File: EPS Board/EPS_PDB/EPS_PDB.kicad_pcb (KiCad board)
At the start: 4 copper layers, 92 x 92 mm, 126 parts, among them J1 USB_B_Micro, J2 Conn_02x26_Odd_Even, J3 Conn_02x26_Odd_Even, J4 Conn_01x04_Pin, Q1 PMOS, Q2 PMOS, SW1 SW_SPDT, U1 AMS1117-3.3, U10 TPS259621DDAT_5V_PAY, U11 LM5000-3MTCX, U12 TPS259621DDAT_5V_EPS, U13 TPS259621DDAT_5V_OBC, U14 AD7708BRUZ, U15 TPS259621DDAT_5V_ADCS, U16 TPS259621DDAT_5V_COMM, U17 LTC3624EMSE-3.3PBF, U18 TPS259621DDAT_12V_ADCS, U19 LTC3624IDD-25PBF, U2 SN65HVD256D, U3 SN65HVD256D, U4 STM32L476VET6, U5 TPS3824-33QDBVRQ1, U6 TS4061BICT-1.25, U7 TPS259621DDAT 3V3_ADCS, U8 TPS259621DDAT_3V3_ANT, U9 TPS259621DDAT_3V3_EPS, Y1 32MHz, Y2 32.768kHz

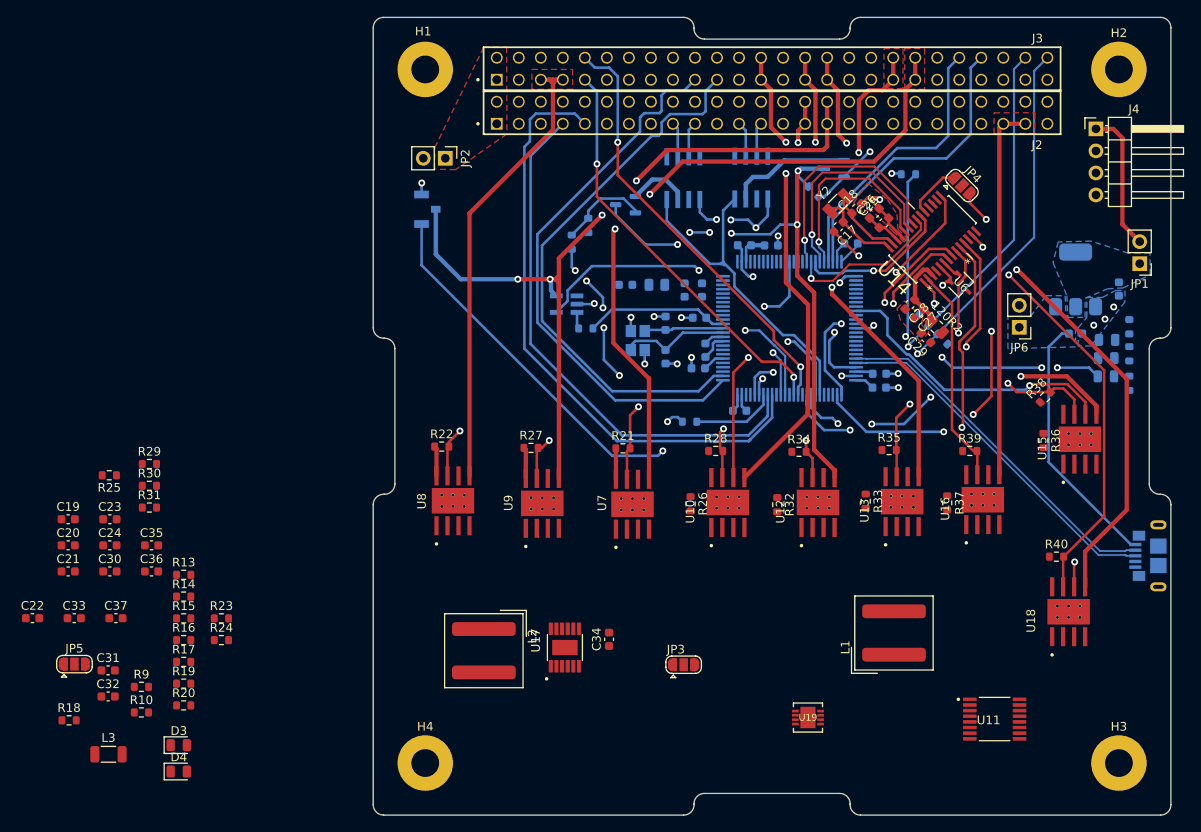
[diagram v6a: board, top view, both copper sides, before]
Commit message: EPS PDB Layout Progress
Voltage Converter layout pending
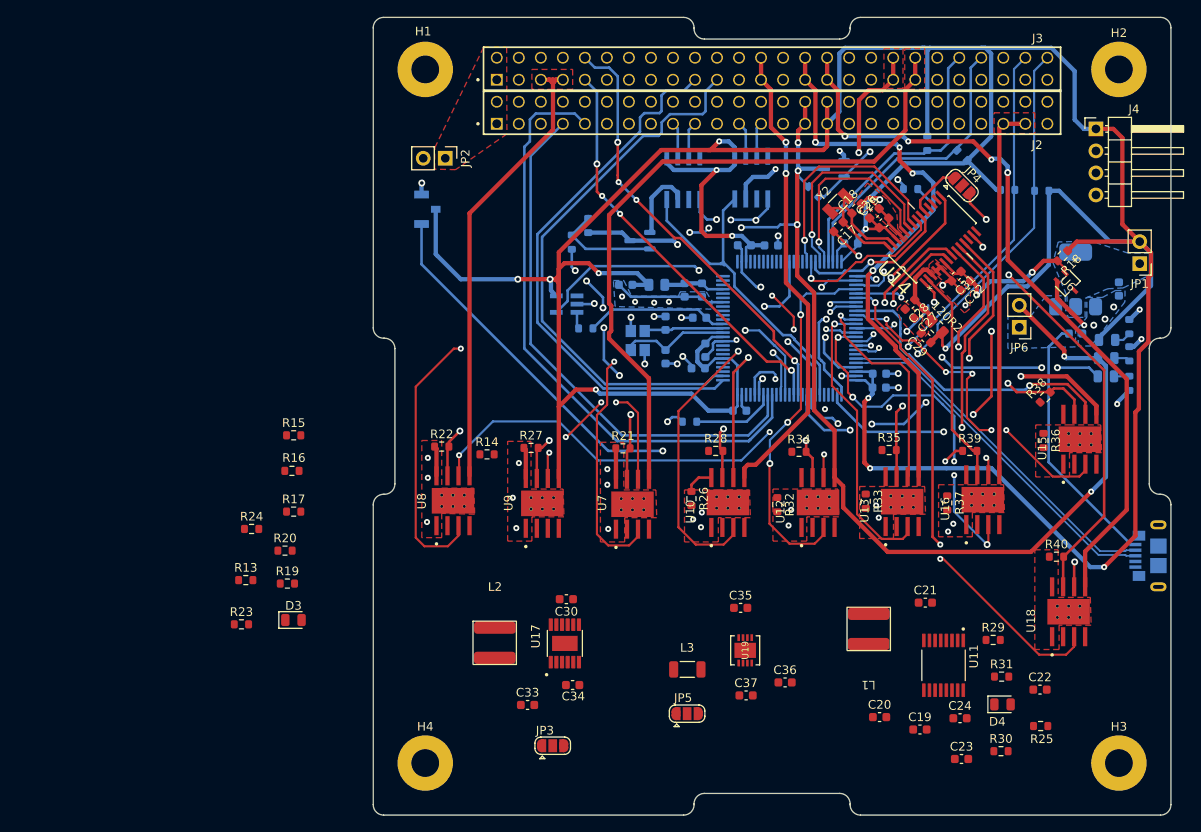
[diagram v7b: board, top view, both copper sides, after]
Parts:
- L1, L2: footprint Inductor_SMD:L_Wuerth_WE-XHMI-8080 -> Inductor-WE-XHMI-5050:WE-XHMI-5050
- R10, R9: moved to B.Cu
- moved R18 126.5 mm to (192.8, 74.2), turned to -135 degrees
- moved C22 116.5 mm to (190.2, 124.2)
- moved R10 114.4 mm to (181.2, 62.6), turned to 135 degrees
- moved R25 111.2 mm to (190.3, 128.4)
- moved R9 110.2 mm to (177.2, 61.2), turned to -90 degrees
- moved C32 109.7 mm to (181.6, 77.6), turned to -135 degrees
- moved C31 107.9 mm to (180.5, 76.5), turned to -135 degrees
- moved R30 102.9 mm to (185.7, 131.3)
- moved C23 102.0 mm to (181.1, 132.2)
- moved C19 101.2 mm to (176.3, 128.8)
- moved R31 100.2 mm to (185.8, 122.7)
- moved C24 100.1 mm to (181.0, 127.5)
- moved R29 99.4 mm to (184.8, 118.5)
- moved C21 98.9 mm to (177.0, 114.2)
- moved C20 95.7 mm to (171.7, 127.4)
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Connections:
- U14 pad 12: GNDA -> GND
- U14 pad 17: GNDA -> GND
- U14 pad 4: GNDA -> GND
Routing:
- net 3V3_EPS: track 130.4 -> 451.4 mm, vias 4 -> 12
- net /EN_3V3_ANT: track 0.00 -> 86.2 mm, vias 0 -> 4
- net 5V_EPS: track 75.6 -> 142.6 mm, vias 7 -> 9
- net /FLT_3V3_ANT: track 0.00 -> 63.1 mm, vias 0 -> 4
- net /EN_3V3_ADCS: track 0.00 -> 59.6 mm, vias 0 -> 2
- net /FLT_12V_ADCS: track 2.90 -> 59.9 mm, vias 1 -> 2
- net /EN_12V_ADCS: track 0.00 -> 56.7 mm, vias 0 -> 3
- net /FLT_5V_EPS: track 0.00 -> 49.2 mm, vias 0 -> 2
- net /EN_5V_PAY: track 0.00 -> 48.9 mm, vias 0 -> 2
- net /FLT_3V3_ADCS: track 0.00 -> 48.8 mm, vias 0 -> 2
- net /FLT_3V3_EPS: track 0.00 -> 44.5 mm, vias 0 -> 4
- net /EN_5V_EPS: track 0.00 -> 42.7 mm, vias 0 -> 3
- net /EN_5V_COMM: track 0.00 -> 42.6 mm, vias 0 -> 5
- net /EN_5V_ADCS: track 0.00 -> 39.4 mm, vias 0 -> 5
- net /EN_5V_OBC: track 0.00 -> 33.9 mm, vias 0 -> 1
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
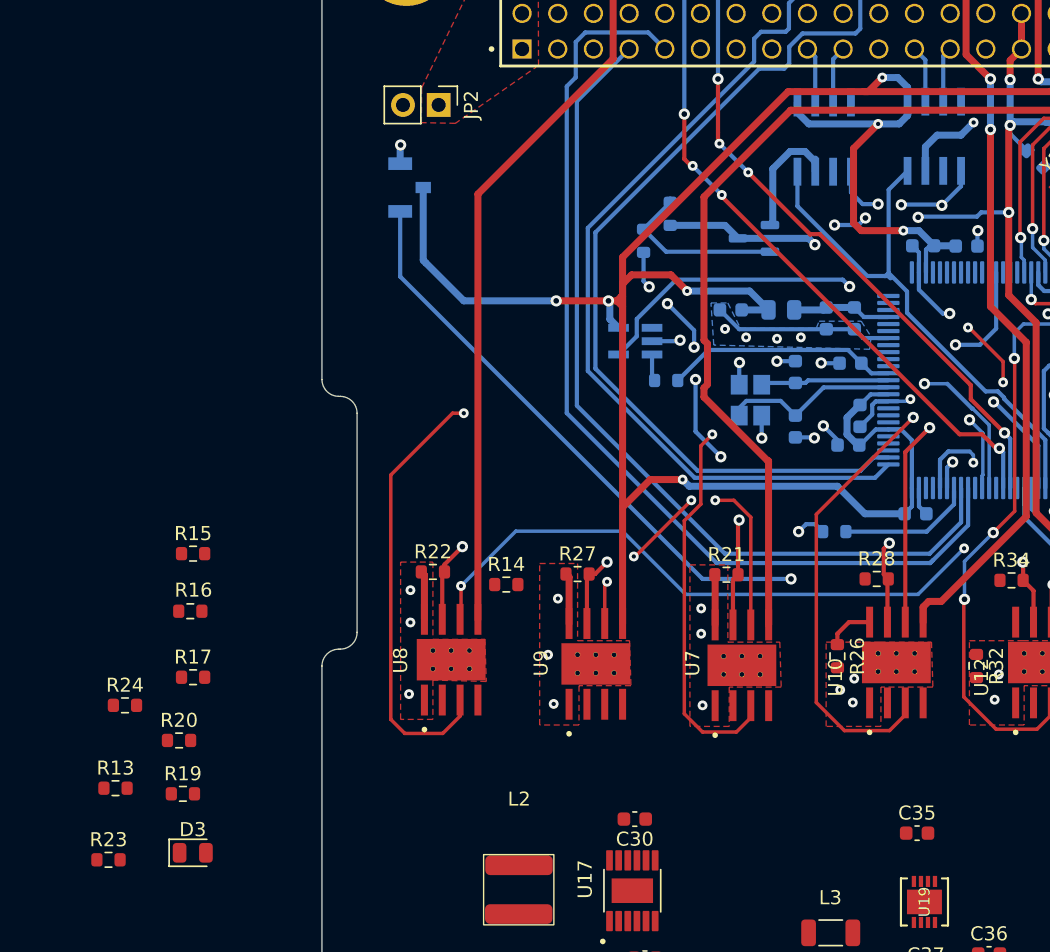
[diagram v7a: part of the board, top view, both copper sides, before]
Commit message: Minor changes in EPS PDB Layout
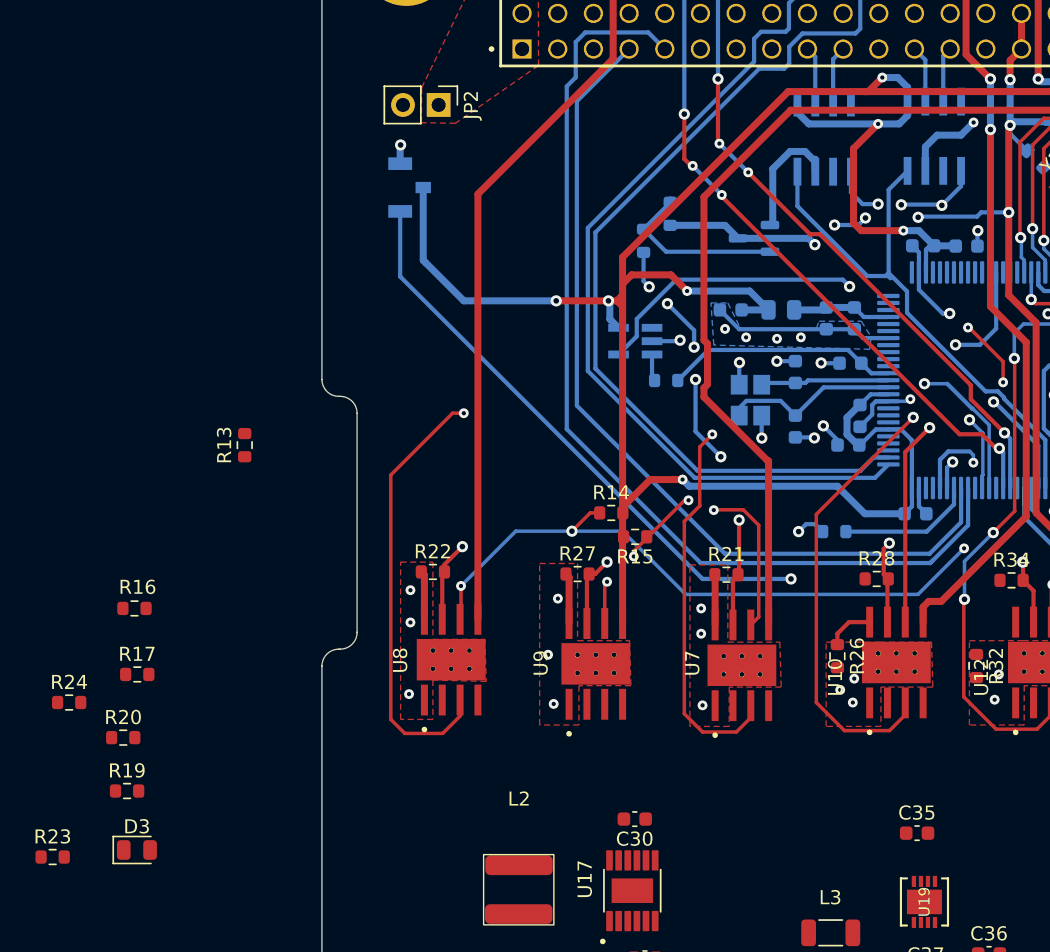
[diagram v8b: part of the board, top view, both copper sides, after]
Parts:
- moved R15 31.5 mm to (135.6, 93.7), turned to 180 degrees
- moved R13 26.1 mm to (107.8, 87.2), turned to 90 degrees
- moved R14 9.05 mm to (133.9, 92.0)
- moved R24 3.98 mm to (95.3, 105.5)
- moved R19 3.98 mm to (99.4, 111.8)
- moved D3 3.98 mm to (100.1, 116.0)
- moved R17 3.98 mm to (100.1, 103.5)
- moved R20 3.98 mm to (99.1, 108.0)
- moved R23 3.98 mm to (94.1, 116.5)
- moved R16 3.98 mm to (99.9, 98.8)
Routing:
- net /FLT_3V3_ANT: track 63.1 -> 65.6 mm, vias 4 -> 5
- net /FLT_3V3_ADCS: track 48.8 -> 49.5 mm
- net /UART1_TX: track 70.8 -> 71.5 mm
- net /EPS Power Distribution/ILM_3V3_ANT: track 72.7 -> 73.3 mm
